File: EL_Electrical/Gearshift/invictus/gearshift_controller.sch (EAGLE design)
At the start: 64 parts, among them IC1 MCP2562-E_SN, IC2 MCP2515-I_SO, Q1 BSS138, Q10 BSS138, Q2 BSS138, Q3 BSS138, Q4 BSS138, Q5 BSS138, Q6 BSS138, Q8 BSS123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

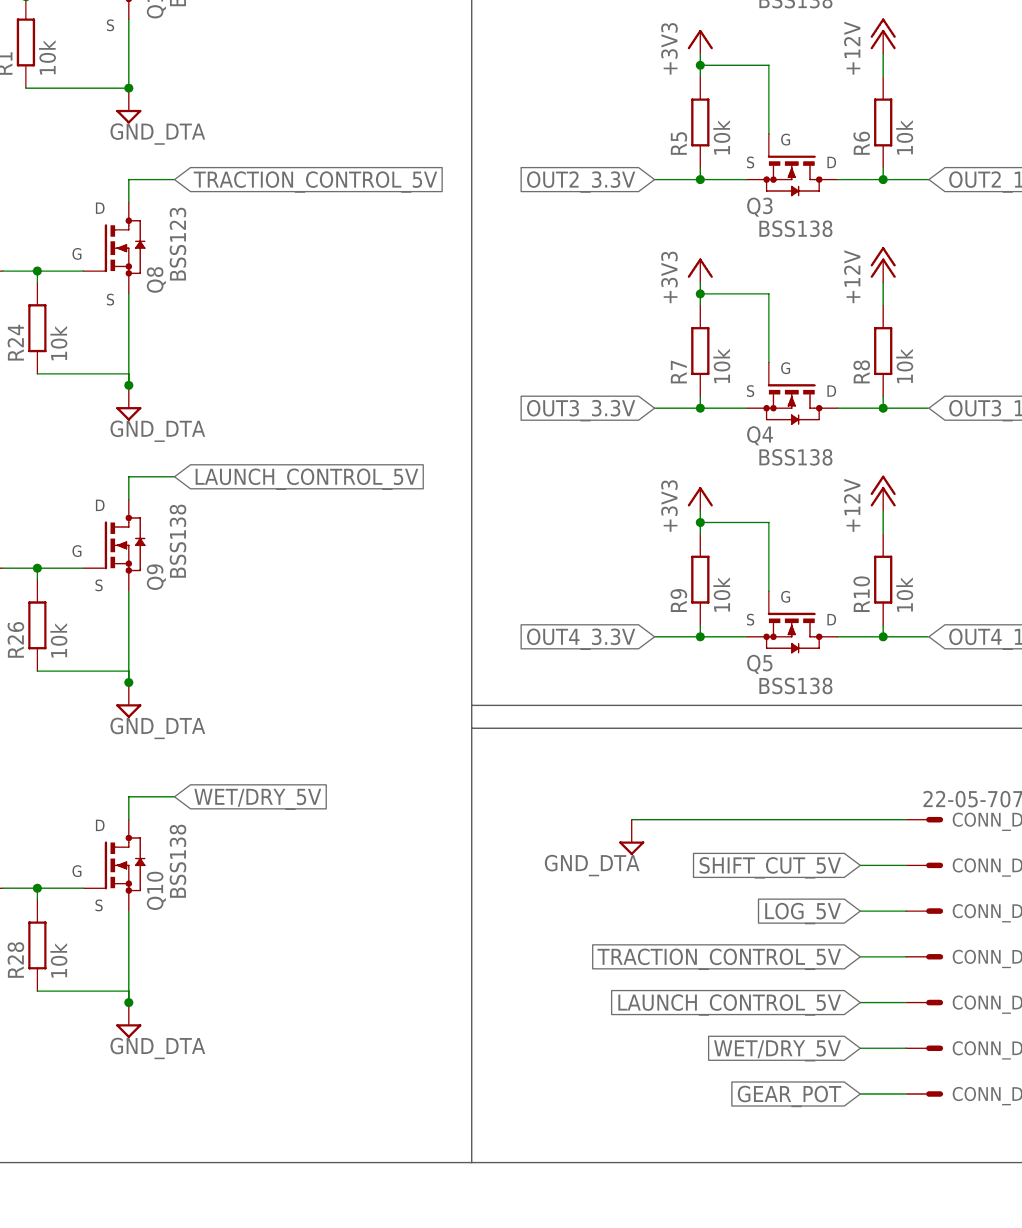
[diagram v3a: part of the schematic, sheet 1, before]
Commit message: Add Bill of Materials (BOM) of gearshift_controller PCB without pinheaders for test points. Minor changes in names
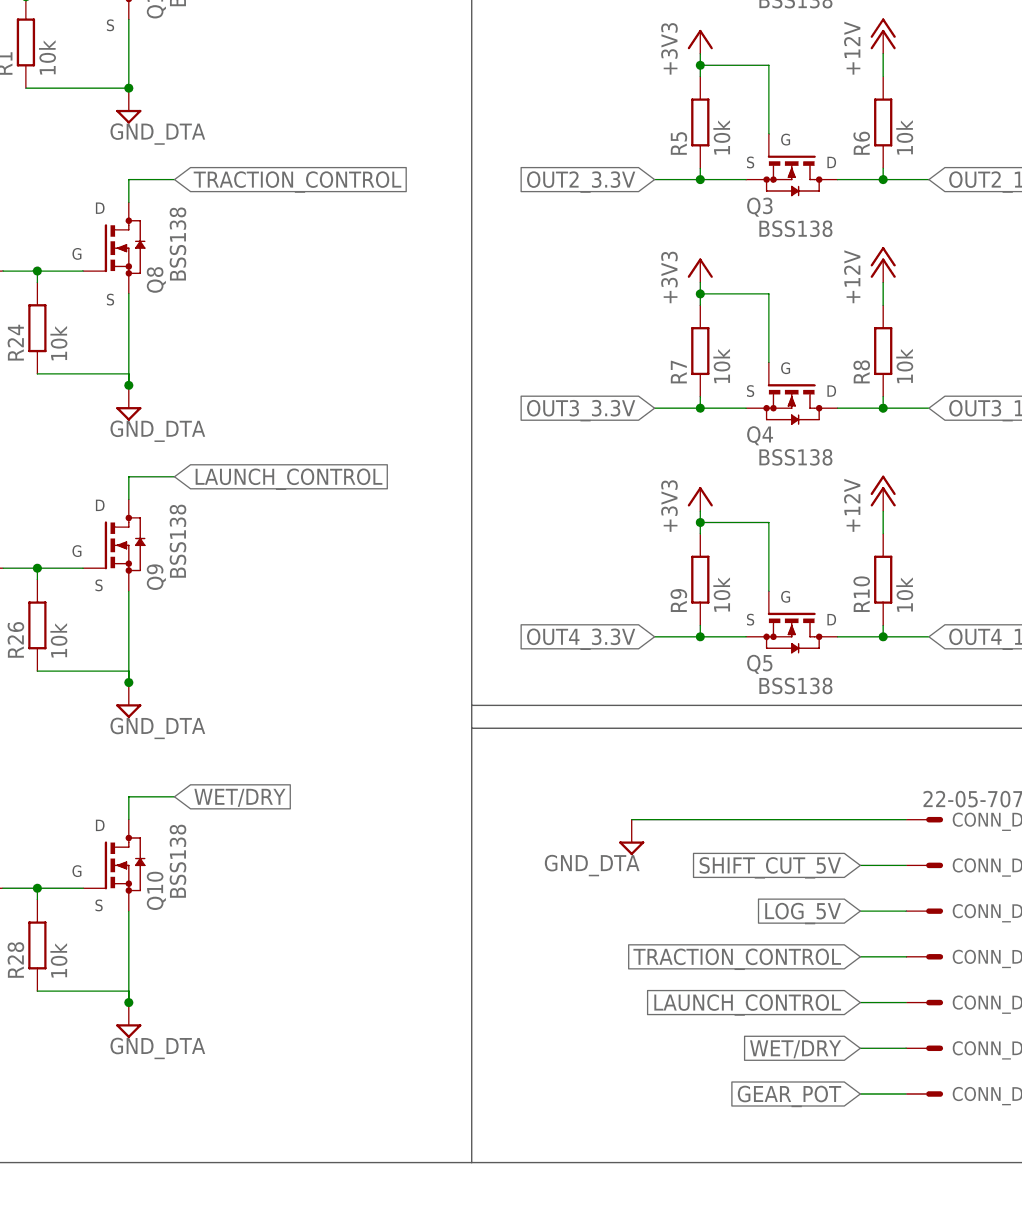
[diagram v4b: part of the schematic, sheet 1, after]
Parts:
- Q8: value BSS123 -> BSS138
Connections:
- net LAUNCH_CONTROL_5V renamed LAUNCH_CONTROL
- net WET/DRY_5V renamed WET/DRY
- new net TRACTION_CONTROL: Q8.D
- net TRACTION_CONTROL_5V: no longer Q8.D
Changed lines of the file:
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@@
 <part name="R2" library="rcl" library_urn="urn:adsk.eagle:library:334" deviceset="R-EU_" device="R0805" package3d_urn="urn:adsk.eagle:package:23553/2" value="4k7"/>
 <part name="P+1" library="supply1" library_urn="urn:adsk.eagle:library:371" deviceset="+5V" device=""/>
-<part name="Q8" library="transistor-small-signal" library_urn="urn:adsk.eagle:library:401" deviceset="BSS123" device="" package3d_urn="urn:adsk.eagle:package:28738/2"/>
+<part name="Q8" library="transistor-small-signal" library_urn="urn:adsk.eagle:library:401" deviceset="BSS123" device="" package3d_urn="urn:adsk.eagle:package:28738/2" value="BSS138"/>
 <part name="R24" library="rcl" library_urn="urn:adsk.eagle:library:334" deviceset="R-EU_" device="R0805" package3d_urn="urn:adsk.eagle:package:23553/2" value="10k"/>
 <part name="R25" library="rcl" library_urn="urn:adsk.eagle:library:334" deviceset="R-EU_" device="R0805" package3d_urn="urn:adsk.eagle:package:23553/2" value="330"/>
@@
 <net name="TRACTION_CONTROL_5V" class="0">
 <segment>
-<pinref part="Q8" gate="G$1" pin="D"/>
-<wire x1="215.9" y1="134.62" x2="215.9" y2="137.16" width="0.1524" layer="91"/>
-<wire x1="220.98" y1="137.16" x2="215.9" y2="137.16" width="0.1524" layer="91"/>
-<label x="220.98" y="137.16" size="1.778" layer="95" xref="yes"/>
-<label x="297.18" y="50.8" size="1.778" layer="95" rot="R180" xref="yes"/>
-</segment>
-<segment>
 <pinref part="CONN_DTA" gate="-4" pin="S"/>
 <wire x1="302.26" y1="50.8" x2="297.18" y2="50.8" width="0.1524" layer="91"/>
@@
 <wire x1="40.64" y1="85.09" x2="40.64" y2="81.28" width="0.1524" layer="91"/>
 <label x="40.64" y="81.28" size="1.778" layer="95" rot="R180" xref="yes"/>
-</segment>
-</net>
-<net name="LAUNCH_CONTROL_5V" class="0">
-<segment>
-<label x="297.18" y="45.72" size="1.778" layer="95" rot="R180" xref="yes"/>
-<pinref part="CONN_DTA" gate="-5" pin="S"/>
-<wire x1="302.26" y1="45.72" x2="297.18" y2="45.72" width="0.1524" layer="91"/>
-</segment>
-<segment>
-<wire x1="220.98" y1="104.14" x2="215.9" y2="104.14" width="0.1524" layer="91"/>
-<pinref part="Q9" gate="G$1" pin="D"/>
-<wire x1="215.9" y1="101.6" x2="215.9" y2="104.14" width="0.1524" layer="91"/>
-<label x="220.98" y="104.14" size="1.778" layer="95" xref="yes"/>
 </segment>
 </net>
@@
 </segment>
 </net>
-<net name="WET/DRY_5V" class="0">
+<net name="LAUNCH_CONTROL" class="0">
+<segment>
+<wire x1="220.98" y1="104.14" x2="215.9" y2="104.14" width="0.1524" layer="91"/>
+<pinref part="Q9" gate="G$1" pin="D"/>
+<wire x1="215.9" y1="101.6" x2="215.9" y2="104.14" width="0.1524" layer="91"/>
+<label x="220.98" y="104.14" size="1.778" layer="95" xref="yes"/>
+</segment>
+<segment>
+<label x="297.18" y="45.72" size="1.778" layer="95" rot="R180" xref="yes"/>
+<pinref part="CONN_DTA" gate="-5" pin="S"/>
+<wire x1="302.26" y1="45.72" x2="297.18" y2="45.72" width="0.1524" layer="91"/>
+</segment>
+</net>
+<net name="WET/DRY" class="0">
 <segment>
 <pinref part="Q10" gate="G$1" pin="D"/>
@@
 </segment>
 </net>
+<net name="TRACTION_CONTROL" class="0">
+<segment>
+<pinref part="Q8" gate="G$1" pin="D"/>
+<wire x1="215.9" y1="134.62" x2="215.9" y2="137.16" width="0.1524" layer="91"/>
+<wire x1="220.98" y1="137.16" x2="215.9" y2="137.16" width="0.1524" layer="91"/>
+<label x="220.98" y="137.16" size="1.778" layer="95" xref="yes"/>
+<label x="297.18" y="50.8" size="1.778" layer="95" rot="R180" xref="yes"/>
+</segment>
+</net>

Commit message: Add test pins
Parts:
- removed JP1, JP2: (no value), jumper:JP2E
- added J_RX_CAN, J_TX_CAN: (no value), jumper:JP2E
- added TEST_DTA: (no value), test_pin_DTA:PINHD-1X6
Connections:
- removed net TRACTION_CONTROL_5V: CONN_DTA-4.S
- net CAN-RXD_SOFTWARE: now also J_RX_CAN.1; no longer JP2.1
- net CAN-RX_HARDWARE: now also J_RX_CAN.3; no longer JP2.3
- net CAN-TXD-SOFTWARE: now also J_TX_CAN.1; no longer JP1.1
- net CAN-TX_HARDWARE: now also J_TX_CAN.3; no longer JP1.3
- net GEAR_POT: now also TEST_DTA.6
- net LAUNCH_CONTROL_3.3V: now also TEST_DTA.4
- net LOG_3.3V: now also TEST_DTA.2
- net RX_CAN: now also J_RX_CAN.2; no longer JP2.2
- net SHIFT_CUT_3.3V: now also TEST_DTA.1
- net TRACTION_CONTROL: now also CONN_DTA-4.S
- net TRACTION_CONTROL_3.3V: now also TEST_DTA.3
- net TX_CAN: now also J_TX_CAN.2; no longer JP1.2
- net WET/DRY_3.3V: now also TEST_DTA.5
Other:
- moved on the sheet: Q1, Q10, Q6, Q8, Q9, R1, R17, R18, R2, R22, R24, R25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

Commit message: Gearshift_controller schematic file (.sch) updade
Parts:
- added GND_DTA: (no value), pinhead:PINHD-1X1
- added TEST_CAN, TEST_PALETTE: (no value), test_pin_DTA:PINHD-1X2
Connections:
- net GND: now also GND_DTA.1
- net N$4: now also TEST_CAN.1
- net N$6: now also TEST_CAN.2
- net PALETTE_DROITE: now also TEST_PALETTE.2
- net PALETTE_GAUCHE: now also TEST_PALETTE.1
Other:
- moved on the sheet: C1, CONN_CAN-1, CONN_CAN-2, CONN_DTA-1, CONN_DTA-2, CONN_DTA-3, CONN_DTA-4, CONN_DTA-5, CONN_DTA-6, CONN_DTA-7, CONN_MOTOR-1, CONN_MOTOR-2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

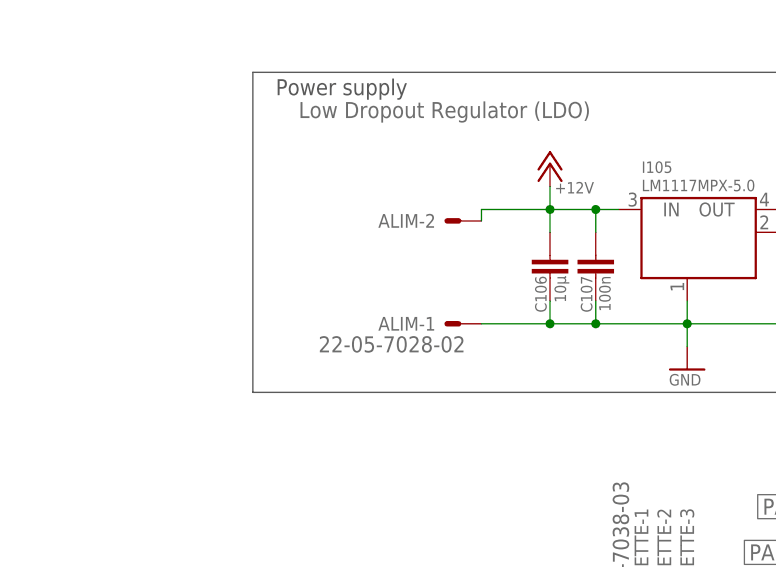
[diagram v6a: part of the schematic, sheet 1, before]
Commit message: Add capacitors (470uF: about 18,20mm x 10,8mm; Footprint utilisé 25mm x 10mm)
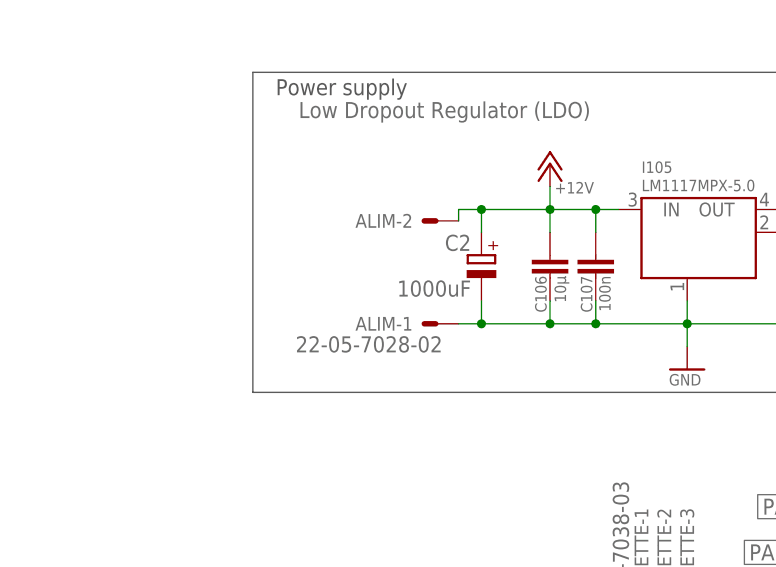
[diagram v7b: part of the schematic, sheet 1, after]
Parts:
- added C2: 1000uF, rcl:CPOL-EUE25-10AXIAL
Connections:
- removed net GND1: CONN_DTA-1.S, Q1.S, Q10.S, Q8.S, Q9.S, R1.1, R24.1, R26.1, R28.1
- net +12V: now also C2.+
- net GND: now also C2.-, CONN_DTA-1.S, Q1.S, Q10.S, Q8.S, Q9.S, R1.1, R24.1, R26.1, R28.1
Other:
- moved on the sheet: ALIM-1, ALIM-2
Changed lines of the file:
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@@
 <part name="TEST_CAN" library="test_pin_DTA" deviceset="PINHD-1X2" device="" package3d_urn="urn:adsk.eagle:package:22435/2"/>
 <part name="TEST_PALETTE" library="test_pin_DTA" deviceset="PINHD-1X2" device="" package3d_urn="urn:adsk.eagle:package:22435/2"/>
+<part name="C2" library="rcl" library_urn="urn:adsk.eagle:library:334" deviceset="CPOL-EU" device="E25-10AXIAL" package3d_urn="urn:adsk.eagle:package:23352/1" value="1000uF"/>
 </parts>
 <sheets>
@@
 <attribute name="VALUE" x="195.58" y="77.978" size="1.778" layer="96"/>
 </instance>
-<instance part="ALIM" gate="-1" x="50.8" y="195.58" smashed="yes" rot="R180">
-<attribute name="NAME" x="48.26" y="196.342" size="1.524" layer="95" rot="R180"/>
-<attribute name="VALUE" x="51.562" y="194.183" size="1.778" layer="96" rot="R180"/>
-</instance>
-<instance part="ALIM" gate="-2" x="50.8" y="207.01" smashed="yes" rot="R180">
-<attribute name="NAME" x="48.26" y="207.772" size="1.524" layer="95" rot="R180"/>
+<instance part="ALIM" gate="-1" x="48.26" y="195.58" smashed="yes" rot="R180">
+<attribute name="NAME" x="45.72" y="196.342" size="1.524" layer="95" rot="R180"/>
+<attribute name="VALUE" x="49.022" y="194.183" size="1.778" layer="96" rot="R180"/>
+</instance>
+<instance part="ALIM" gate="-2" x="48.26" y="207.01" smashed="yes" rot="R180">
+<attribute name="NAME" x="45.72" y="207.772" size="1.524" layer="95" rot="R180"/>
 </instance>
 <instance part="CONN_MOTOR" gate="-1" x="353.06" y="93.98" smashed="yes">
@@
 <attribute name="NAME" x="102.87" y="178.435" size="1.778" layer="95"/>
 <attribute name="VALUE" x="107.95" y="167.64" size="1.778" layer="96"/>
+</instance>
+<instance part="C2" gate="G$1" x="53.34" y="203.2" smashed="yes" rot="MR0">
+<attribute name="NAME" x="52.197" y="203.6826" size="1.778" layer="95" rot="MR0"/>
+<attribute name="VALUE" x="52.197" y="198.6026" size="1.778" layer="96" rot="MR0"/>
 </instance>
 </instances>
@@
 <pinref part="P+11" gate="1" pin="+12V"/>
 <pinref part="ALIM" gate="-2" pin="S"/>
-<wire x1="53.34" y1="207.01" x2="53.34" y2="208.28" width="0.1524" layer="91"/>
+<wire x1="50.8" y1="207.01" x2="50.8" y2="208.28" width="0.1524" layer="91"/>
+<wire x1="50.8" y1="208.28" x2="53.34" y2="208.28" width="0.1524" layer="91"/>
+<pinref part="C2" gate="G$1" pin="+"/>
 <wire x1="53.34" y1="208.28" x2="60.96" y2="208.28" width="0.1524" layer="91"/>
+<wire x1="53.34" y1="205.74" x2="53.34" y2="208.28" width="0.1524" layer="91"/>
+<junction x="53.34" y="208.28"/>
 </segment>
 </net>
@@
 <wire x1="60.96" y1="195.58" x2="53.34" y2="195.58" width="0.1524" layer="91"/>
 <junction x="60.96" y="195.58"/>
+<pinref part="C2" gate="G$1" pin="-"/>
+<wire x1="53.34" y1="195.58" x2="50.8" y2="195.58" width="0.1524" layer="91"/>
+<wire x1="53.34" y1="198.12" x2="53.34" y2="195.58" width="0.1524" layer="91"/>
+<junction x="53.34" y="195.58"/>
 </segment>
 <segment>
@@
 <wire x1="238.76" y1="35.56" x2="238.76" y2="38.1" width="0.1524" layer="91"/>
 <junction x="238.76" y="38.1"/>
+</segment>
+<segment>
+<pinref part="CONN_DTA" gate="-1" pin="S"/>
+<pinref part="SUPPLY1" gate="G$1" pin="GND1"/>
+<wire x1="302.26" y1="93.98" x2="271.78" y2="93.98" width="0.1524" layer="91"/>
+</segment>
+<segment>
+<pinref part="R28" gate="G$1" pin="1"/>
+<pinref part="SUPPLY5" gate="G$1" pin="GND1"/>
+<wire x1="208.28" y1="69.85" x2="218.44" y2="69.85" width="0.1524" layer="91"/>
+<wire x1="218.44" y1="69.85" x2="218.44" y2="68.58" width="0.1524" layer="91"/>
+<pinref part="Q10" gate="G$1" pin="S"/>
+<wire x1="218.44" y1="68.58" x2="218.44" y2="78.74" width="0.1524" layer="91"/>
+<junction x="218.44" y="68.58"/>
+</segment>
+<segment>
+<pinref part="R26" gate="G$1" pin="1"/>
+<pinref part="SUPPLY4" gate="G$1" pin="GND1"/>
+<wire x1="208.28" y1="105.41" x2="218.44" y2="105.41" width="0.1524" layer="91"/>
+<wire x1="218.44" y1="105.41" x2="218.44" y2="104.14" width="0.1524" layer="91"/>
+<pinref part="Q9" gate="G$1" pin="S"/>
+<wire x1="218.44" y1="104.14" x2="218.44" y2="114.3" width="0.1524" layer="91"/>
+<junction x="218.44" y="104.14"/>
+</segment>
+<segment>
+<pinref part="Q1" gate="G$1" pin="S"/>
+<pinref part="R1" gate="G$1" pin="1"/>
+<wire x1="218.44" y1="177.8" x2="218.44" y2="170.18" width="0.1524" layer="91"/>
+<wire x1="218.44" y1="170.18" x2="207.01" y2="170.18" width="0.1524" layer="91"/>
+<pinref part="SUPPLY2" gate="G$1" pin="GND1"/>
+<junction x="218.44" y="170.18"/>
+</segment>
+<segment>
+<pinref part="R24" gate="G$1" pin="1"/>
+<pinref part="SUPPLY3" gate="G$1" pin="GND1"/>
+<wire x1="208.28" y1="138.43" x2="218.44" y2="138.43" width="0.1524" layer="91"/>
+<wire x1="218.44" y1="138.43" x2="218.44" y2="137.16" width="0.1524" layer="91"/>
+<pinref part="Q8" gate="G$1" pin="S"/>
+<wire x1="218.44" y1="137.16" x2="218.44" y2="147.32" width="0.1524" layer="91"/>
+<junction x="218.44" y="137.16"/>
 </segment>
 </net>
@@
 </segment>
 </net>
-<net name="GND1" class="0">
-<segment>
-<pinref part="Q1" gate="G$1" pin="S"/>
-<pinref part="R1" gate="G$1" pin="1"/>
-<wire x1="218.44" y1="177.8" x2="218.44" y2="170.18" width="0.1524" layer="91"/>
-<wire x1="218.44" y1="170.18" x2="207.01" y2="170.18" width="0.1524" layer="91"/>
-<pinref part="SUPPLY2" gate="G$1" pin="GND1"/>
-<junction x="218.44" y="170.18"/>
-</segment>
-<segment>
-<pinref part="R26" gate="G$1" pin="1"/>
-<pinref part="SUPPLY4" gate="G$1" pin="GND1"/>
-<wire x1="208.28" y1="105.41" x2="218.44" y2="105.41" width="0.1524" layer="91"/>
-<wire x1="218.44" y1="105.41" x2="218.44" y2="104.14" width="0.1524" layer="91"/>
-<pinref part="Q9" gate="G$1" pin="S"/>
-<wire x1="218.44" y1="104.14" x2="218.44" y2="114.3" width="0.1524" layer="91"/>
-<junction x="218.44" y="104.14"/>
-</segment>
-<segment>
-<pinref part="R28" gate="G$1" pin="1"/>
-<pinref part="SUPPLY5" gate="G$1" pin="GND1"/>
-<wire x1="208.28" y1="69.85" x2="218.44" y2="69.85" width="0.1524" layer="91"/>
-<wire x1="218.44" y1="69.85" x2="218.44" y2="68.58" width="0.1524" layer="91"/>
-<pinref part="Q10" gate="G$1" pin="S"/>
-<wire x1="218.44" y1="68.58" x2="218.44" y2="78.74" width="0.1524" layer="91"/>
-<junction x="218.44" y="68.58"/>
-</segment>
-<segment>
-<pinref part="R24" gate="G$1" pin="1"/>
-<pinref part="SUPPLY3" gate="G$1" pin="GND1"/>
-<wire x1="208.28" y1="138.43" x2="218.44" y2="138.43" width="0.1524" layer="91"/>
-<wire x1="218.44" y1="138.43" x2="218.44" y2="137.16" width="0.1524" layer="91"/>
-<pinref part="Q8" gate="G$1" pin="S"/>
-<wire x1="218.44" y1="137.16" x2="218.44" y2="147.32" width="0.1524" layer="91"/>
-<junction x="218.44" y="137.16"/>
-</segment>
-<segment>
-<pinref part="CONN_DTA" gate="-1" pin="S"/>
-<pinref part="SUPPLY1" gate="G$1" pin="GND1"/>
-<wire x1="302.26" y1="93.98" x2="271.78" y2="93.98" width="0.1524" layer="91"/>
-</segment>
-</net>

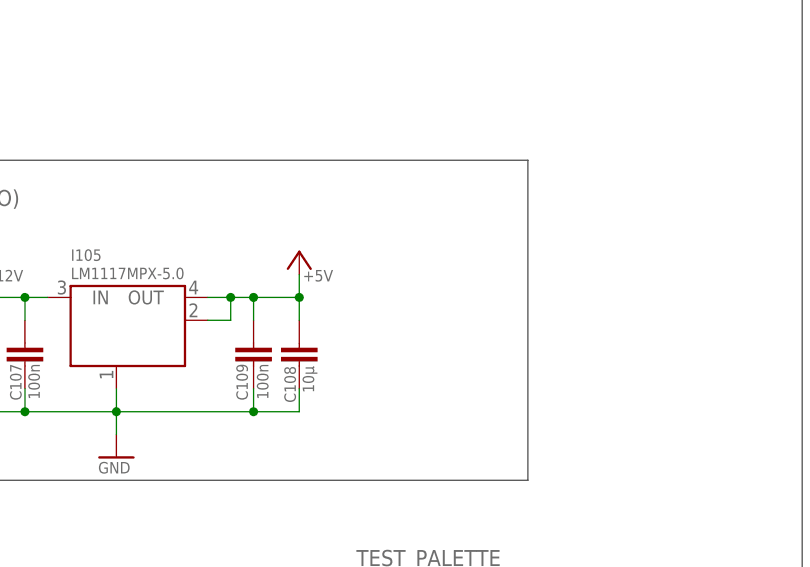
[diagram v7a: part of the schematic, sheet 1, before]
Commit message: Delete useless resistors (Dashboard_controller)
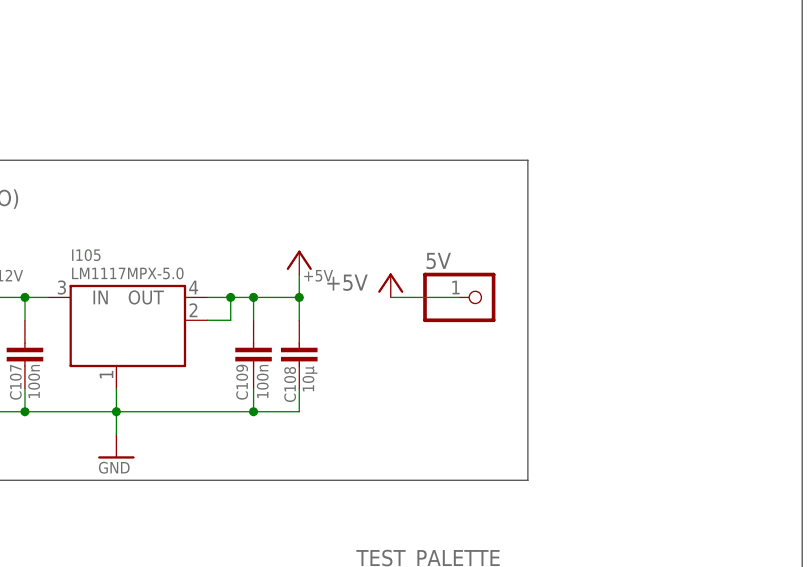
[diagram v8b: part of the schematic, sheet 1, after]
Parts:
- added 5V: (no value), pinhead:PINHD-1X1
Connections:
- net +5V: now also 5V.1
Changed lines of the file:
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@@
 <part name="TEST_PALETTE" library="test_pin_DTA" deviceset="PINHD-1X2" device="" package3d_urn="urn:adsk.eagle:package:22435/2"/>
 <part name="C2" library="rcl" library_urn="urn:adsk.eagle:library:334" deviceset="CPOL-EU" device="E25-10AXIAL" package3d_urn="urn:adsk.eagle:package:23352/1" value="1000uF"/>
+<part name="P+6" library="supply1" library_urn="urn:adsk.eagle:library:371" deviceset="+5V" device=""/>
+<part name="5V" library="pinhead" library_urn="urn:adsk.eagle:library:325" deviceset="PINHD-1X1" device="" package3d_urn="urn:adsk.eagle:package:22485/2"/>
 </parts>
 <sheets>
@@
 <attribute name="VALUE" x="52.197" y="198.6026" size="1.778" layer="96" rot="MR0"/>
 </instance>
+<instance part="P+6" gate="1" x="106.68" y="210.82" smashed="yes">
+<attribute name="VALUE" x="104.14" y="210.82" size="1.778" layer="96" rot="R180"/>
+</instance>
+<instance part="5V" gate="G$1" x="116.84" y="208.28" smashed="yes">
+<attribute name="NAME" x="110.49" y="211.455" size="1.778" layer="95"/>
+<attribute name="VALUE" x="110.49" y="203.2" size="1.778" layer="96"/>
+</instance>
 </instances>
 <busses>
@@
 <pinref part="P+1" gate="1" pin="+5V"/>
 </segment>
-</net>
+<segment>
+<pinref part="5V" gate="G$1" pin="1"/>
+<pinref part="P+6" gate="1" pin="+5V"/>
+<wire x1="114.3" y1="208.28" x2="106.68" y2="208.28" width="0.1524" layer="91"/>
+</segment>
+</net>
